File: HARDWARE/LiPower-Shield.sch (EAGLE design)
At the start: 52 parts, among them U1 MAX17043G+U, U2 TPS61200, U3 MCP73831, U4 ARDUINO_R3_SHIELD, X1 USBSMD

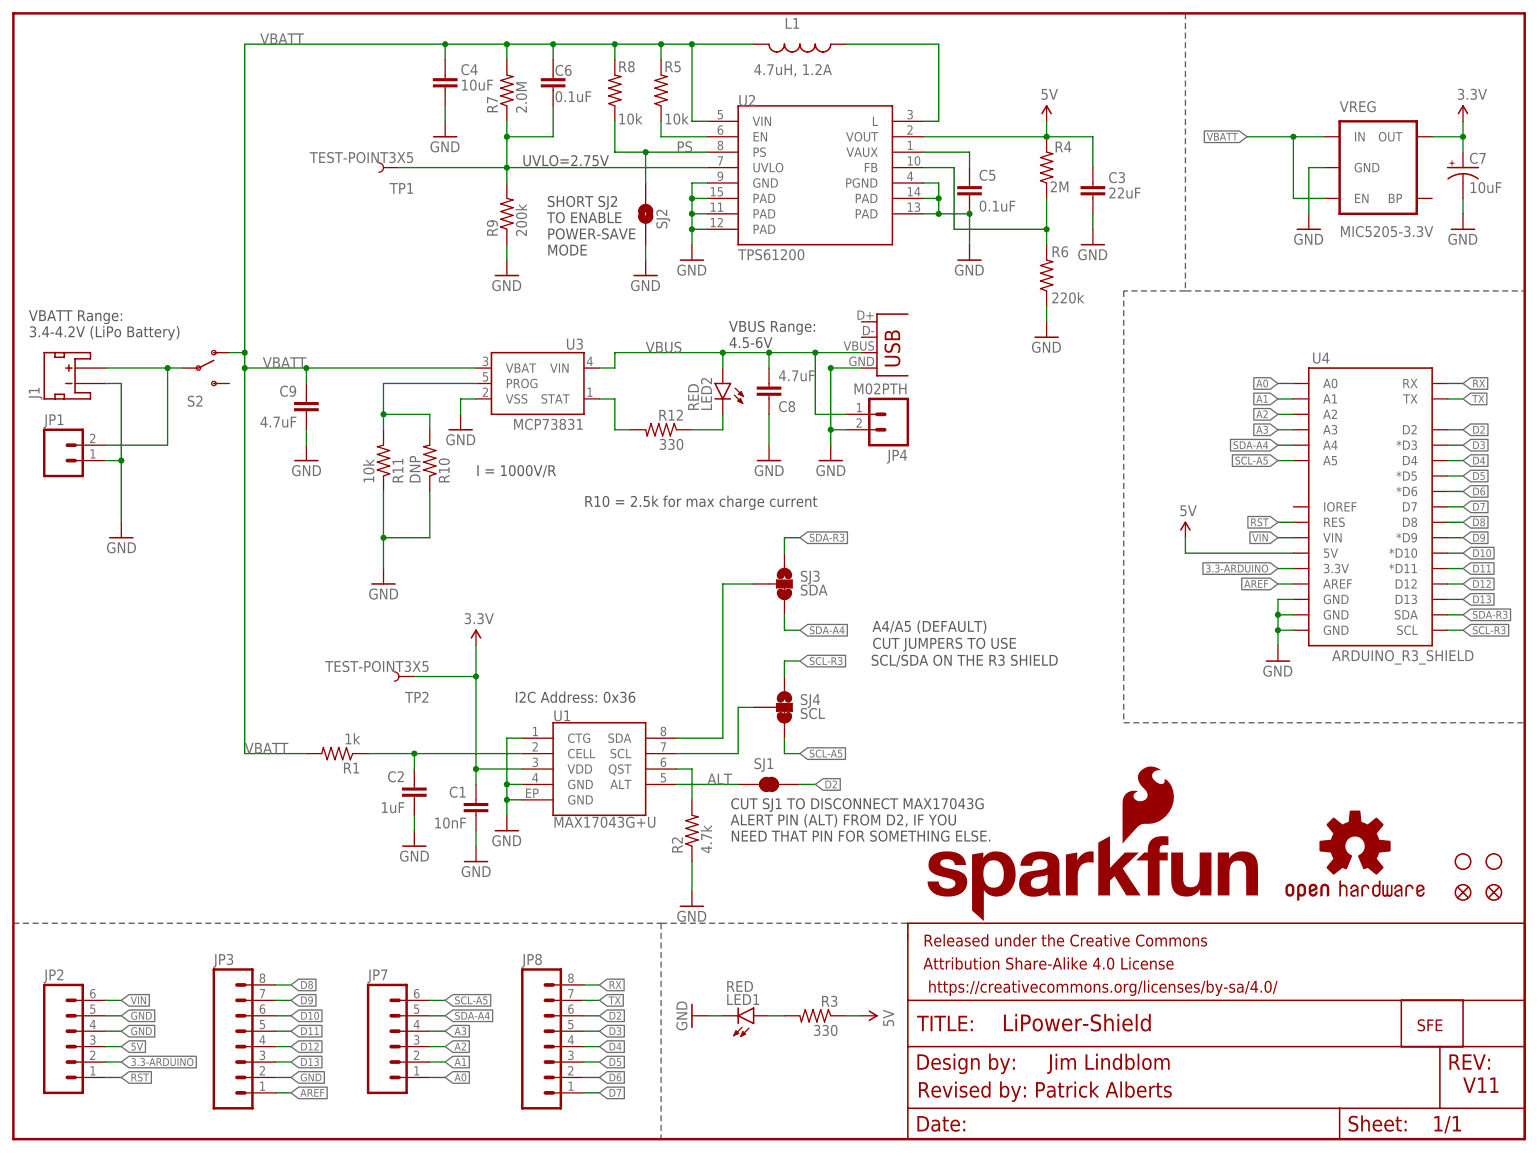
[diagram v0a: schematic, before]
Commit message: Schematic Cleanup
fixed all of these...

1) GND and 5V symbols need to be rotated "up" and "down".

2) all LEDs prefixes should be "D#"

3) R4 needs to be shifted down one grid space. The resulting 4 way
junction will need to be fixed then too.

4) J1 should have a prefix of JP#

5) USB connector is currently "X1" should be a JP prefix.

6) small flame symbol needs to be updated.
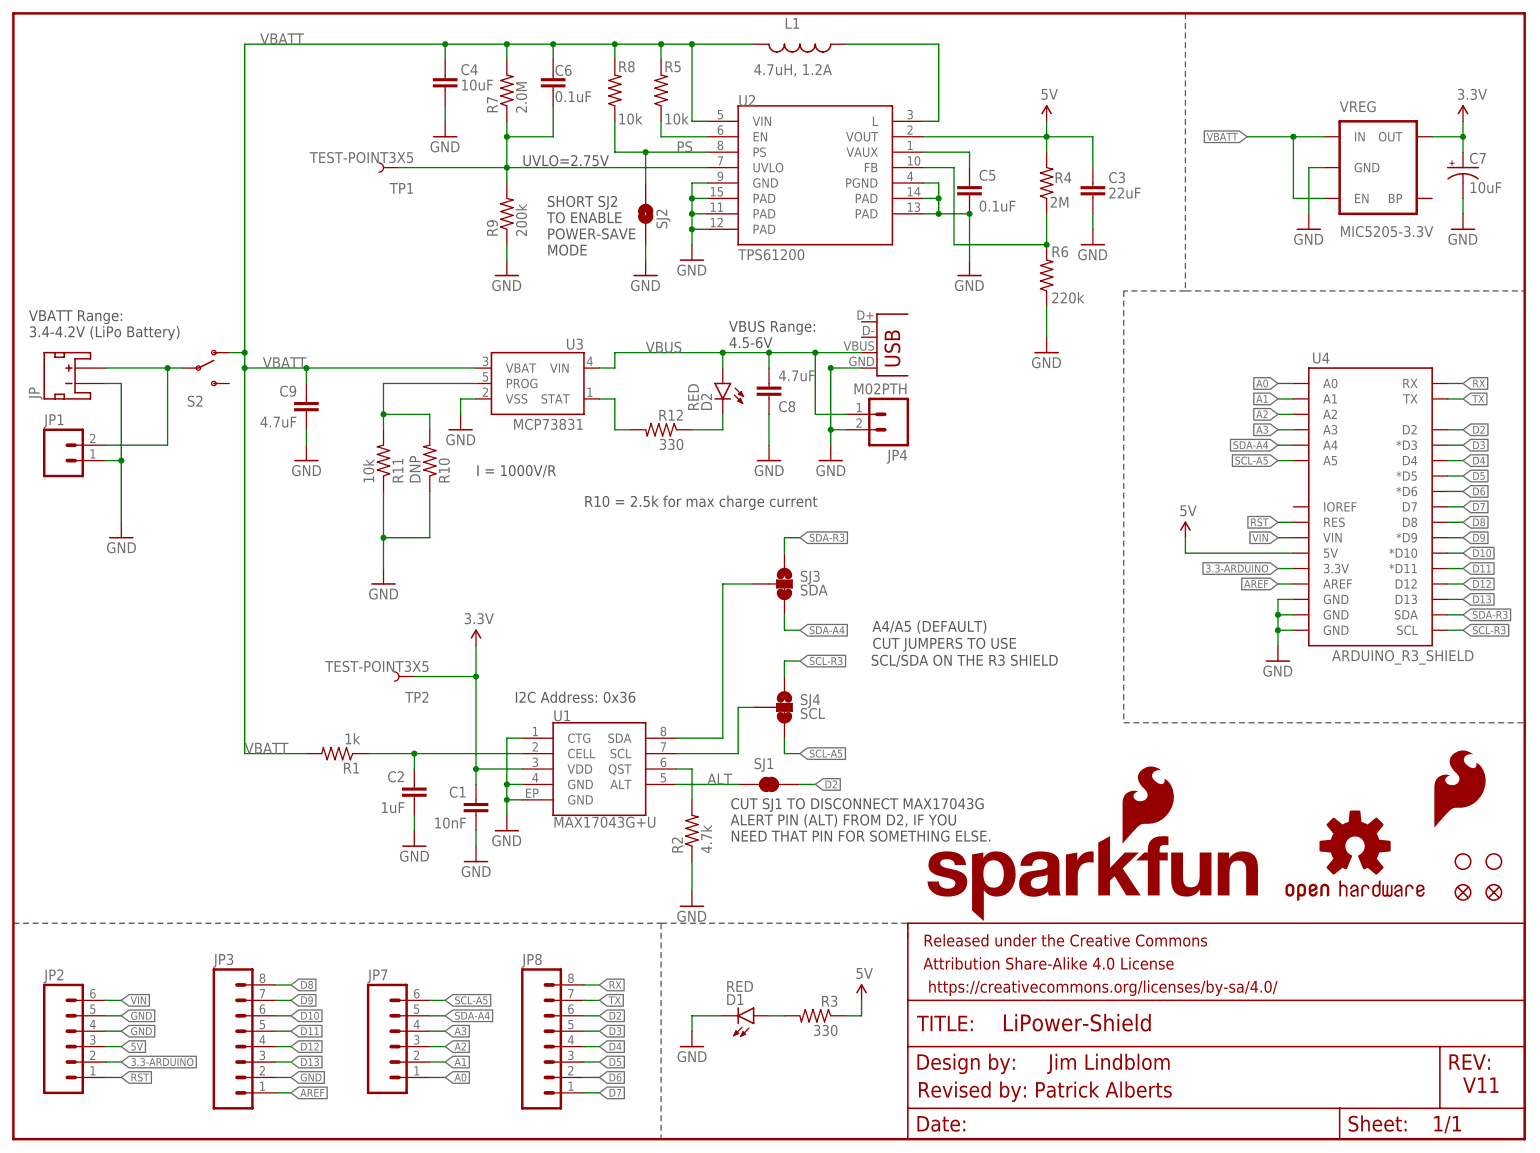
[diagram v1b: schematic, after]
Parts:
- removed JP100: LOGO-SFESK, SparkFun:LOGO-SFESK
- added LOGO3: SFE_LOGO_FLAME.1_INCH, SparkFun-Aesthetics:SFE_LOGO_FLAME.1_INCH
- renumbered J1 to JP, LED1 to D1, LED2 to D2, X1 to JP11
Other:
- moved on the sheet: R4

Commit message: changed fids to regular from micro
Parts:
- removed JP5, JP6: FIDUCIAL1X2.5, abes:FIDUCIAL1X2.5
- added FID1, FID2: FIDUCIAL1X2, SparkFun-Aesthetics:FIDUCIAL1X2
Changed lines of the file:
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@@
 <?xml version="1.0" encoding="utf-8"?>
 <!DOCTYPE eagle SYSTEM "eagle.dtd">
-<eagle version="6.4">
+<eagle version="6.6.0">
 <drawing>
 <settings>
@@
 <part name="SJ2" library="SparkFun" deviceset="SOLDERJUMPER" device="NO" value="PS"/>
 <part name="GND17" library="SparkFun" deviceset="GND" device=""/>
-<part name="JP5" library="abes" deviceset="FIDUCIAL" device="1X2.5"/>
-<part name="JP6" library="abes" deviceset="FIDUCIAL" device="1X2.5"/>
 <part name="JP" library="SparkFun-Connectors" deviceset="JST_2MM_MALE" device=""/>
 <part name="TP1" library="SparkFun-Passives" deviceset="TEST-POINT" device="3X5"/>
@@
 <part name="JP10" library="SparkFun" deviceset="STAND-OFF" device="TIGHT"/>
 <part name="LOGO3" library="SparkFun-Aesthetics" deviceset="SFE_LOGO_FLAME" device=".1_INCH"/>
+<part name="FID1" library="SparkFun-Aesthetics" deviceset="FIDUCIAL" device="1X2"/>
+<part name="FID2" library="SparkFun-Aesthetics" deviceset="FIDUCIAL" device="1X2"/>
 </parts>
 <sheets>
@@
 </instance>
 <instance part="GND17" gate="1" x="104.14" y="142.24"/>
-<instance part="JP5" gate="G$1" x="243.84" y="40.64"/>
-<instance part="JP6" gate="G$1" x="238.76" y="40.64"/>
 <instance part="JP" gate="G$1" x="10.16" y="124.46" rot="R90"/>
 <instance part="TP1" gate="G$1" x="63.5" y="160.02" rot="R180"/>
@@
 <instance part="JP10" gate="G$1" x="243.84" y="45.72"/>
 <instance part="LOGO3" gate="G$1" x="233.68" y="50.8"/>
+<instance part="FID1" gate="G$1" x="238.76" y="40.64"/>
+<instance part="FID2" gate="G$1" x="243.84" y="40.64"/>
 </instances>
 <busses>

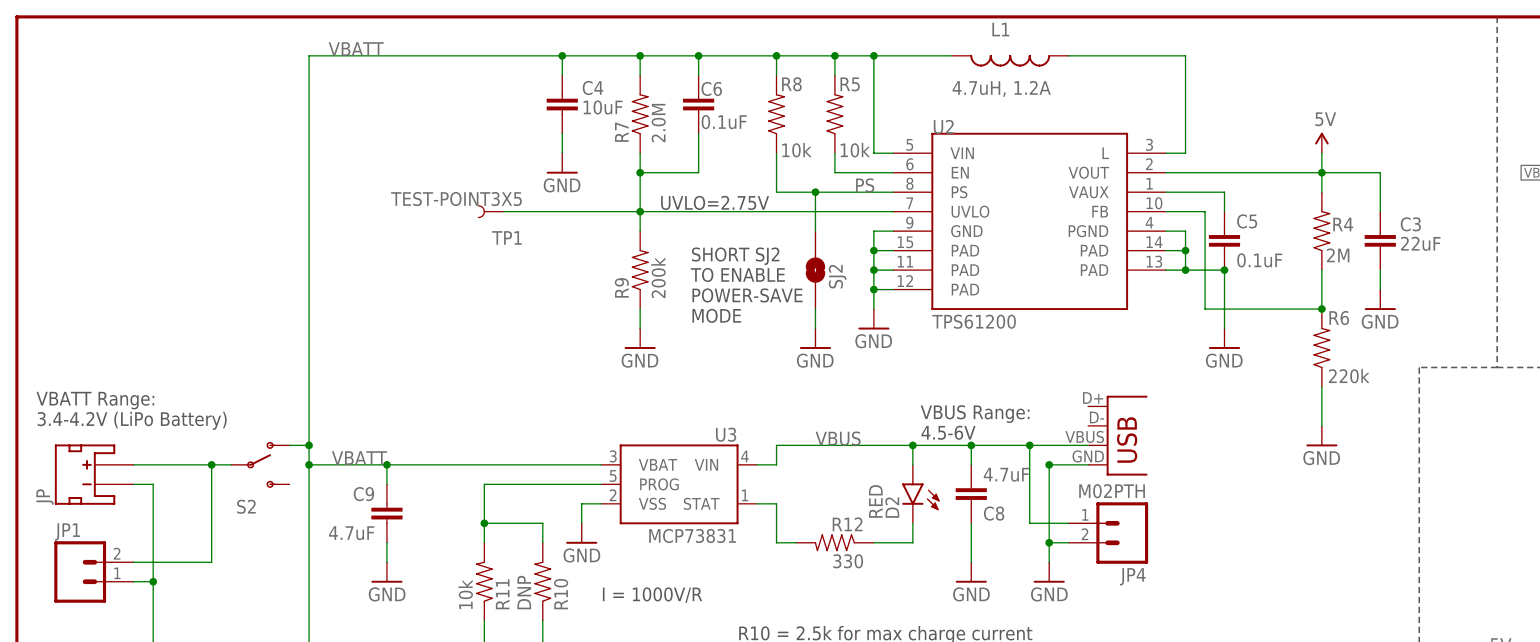
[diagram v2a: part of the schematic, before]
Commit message: Fixed current QC checklist issues.
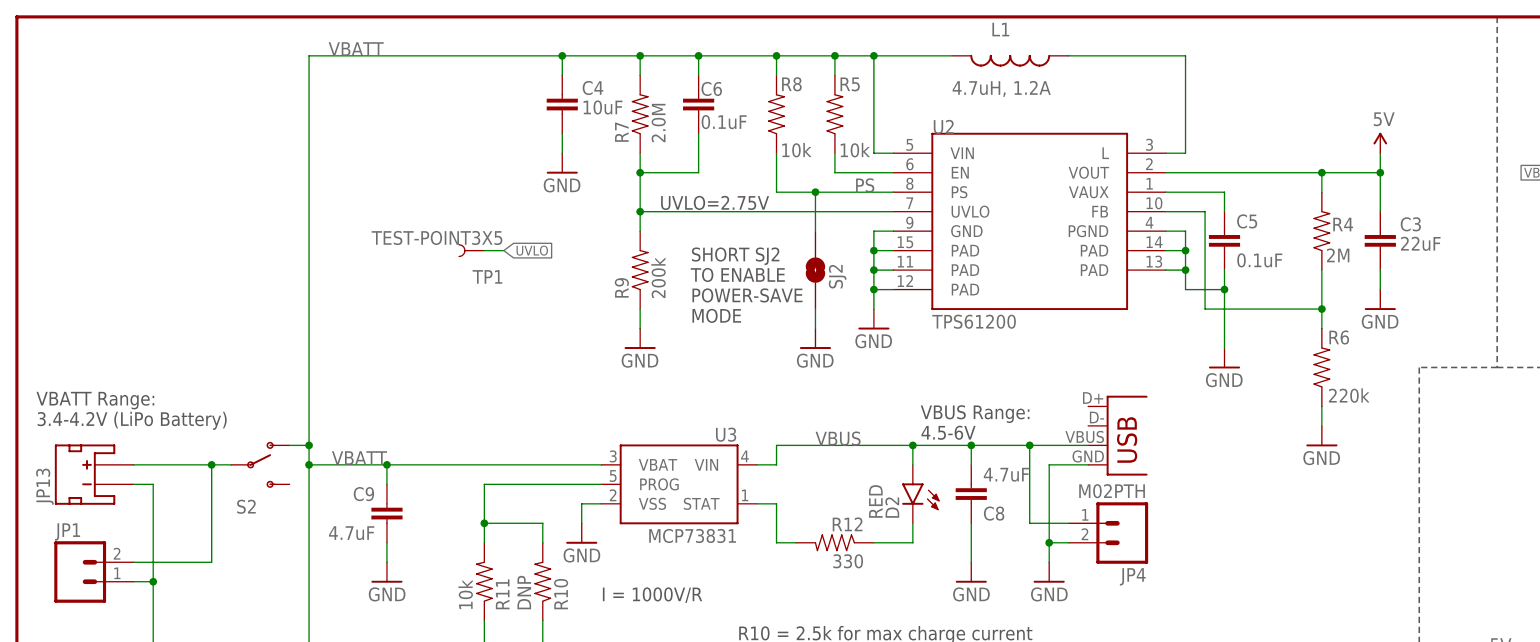
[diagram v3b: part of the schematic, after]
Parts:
- renumbered JP to JP13
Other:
- moved on the sheet: R6, TP1
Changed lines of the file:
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@@
 <?xml version="1.0" encoding="utf-8"?>
 <!DOCTYPE eagle SYSTEM "eagle.dtd">
-<eagle version="6.6.0">
+<eagle version="6.4">
 <drawing>
 <settings>
@@
 <part name="R5" library="SparkFun-Resistors" deviceset="10KOHM1/10W1%(0603)" device="0603" value="10k"/>
 <part name="R8" library="SparkFun-Resistors" deviceset="10KOHM1/10W1%(0603)" device="0603" value="10k"/>
-<part name="U$4" library="SparkFun" deviceset="5V" device=""/>
 <part name="SJ2" library="SparkFun" deviceset="SOLDERJUMPER" device="NO" value="PS"/>
 <part name="GND17" library="SparkFun" deviceset="GND" device=""/>
-<part name="JP" library="SparkFun-Connectors" deviceset="JST_2MM_MALE" device=""/>
+<part name="JP13" library="SparkFun-Connectors" deviceset="JST_2MM_MALE" device=""/>
 <part name="TP1" library="SparkFun-Passives" deviceset="TEST-POINT" device="3X5"/>
 <part name="LOGO1" library="SparkFun-Aesthetics" deviceset="OSHW-LOGO" device="S"/>
@@
 <part name="FID1" library="SparkFun-Aesthetics" deviceset="FIDUCIAL" device="1X2"/>
 <part name="FID2" library="SparkFun-Aesthetics" deviceset="FIDUCIAL" device="1X2"/>
+<part name="U$2" library="SparkFun" deviceset="5V" device=""/>
 </parts>
 <sheets>
@@
 </instance>
 <instance part="C5" gate="G$1" x="157.48" y="154.94"/>
-<instance part="R6" gate="G$1" x="170.18" y="142.24" smashed="yes" rot="R90">
-<attribute name="NAME" x="170.942" y="145.2626" size="1.778" layer="95"/>
-<attribute name="VALUE" x="170.942" y="137.668" size="1.778" layer="96"/>
+<instance part="R6" gate="G$1" x="170.18" y="139.7" smashed="yes" rot="R90">
+<attribute name="NAME" x="170.942" y="142.7226" size="1.778" layer="95"/>
+<attribute name="VALUE" x="170.942" y="135.128" size="1.778" layer="96"/>
 </instance>
 <instance part="GND4" gate="1" x="177.8" y="147.32"/>
@@
 <attribute name="VALUE" x="73.66" y="172.72" size="1.778" layer="96"/>
 </instance>
-<instance part="GND5" gate="1" x="157.48" y="142.24"/>
+<instance part="GND5" gate="1" x="157.48" y="139.7"/>
 <instance part="GND6" gate="1" x="111.76" y="144.78"/>
 <instance part="GND16" gate="1" x="71.12" y="165.1"/>
@@
 <attribute name="VALUE" x="99.568" y="167.132" size="1.778" layer="96"/>
 </instance>
-<instance part="U$4" gate="G$1" x="170.18" y="167.64"/>
 <instance part="SJ2" gate="1" x="104.14" y="152.4" smashed="yes" rot="R90">
 <attribute name="NAME" x="107.696" y="149.86" size="1.778" layer="95" rot="R90"/>
 </instance>
 <instance part="GND17" gate="1" x="104.14" y="142.24"/>
-<instance part="JP" gate="G$1" x="10.16" y="124.46" rot="R90"/>
-<instance part="TP1" gate="G$1" x="63.5" y="160.02" rot="R180"/>
+<instance part="JP13" gate="G$1" x="10.16" y="124.46" rot="R90"/>
+<instance part="TP1" gate="G$1" x="60.96" y="154.94" rot="R180"/>
 <instance part="LOGO1" gate="G$1" x="220.98" y="48.26"/>
 <instance part="LOGO2" gate="G$1" x="149.86" y="35.56"/>
@@
 <instance part="FID1" gate="G$1" x="238.76" y="40.64"/>
 <instance part="FID2" gate="G$1" x="243.84" y="40.64"/>
+<instance part="U$2" gate="G$1" x="177.8" y="167.64"/>
 </instances>
 <busses>
@@
 <wire x1="134.62" y1="116.84" x2="134.62" y2="127" width="0.1524" layer="91"/>
 <wire x1="137.16" y1="116.84" x2="134.62" y2="116.84" width="0.1524" layer="91"/>
-<junction x="134.62" y="127"/>
 <junction x="134.62" y="116.84"/>
 <pinref part="JP11" gate="G$1" pin="GND"/>
@@
 <pinref part="GND13" gate="1" pin="GND"/>
 <pinref part="JP1" gate="G$1" pin="1"/>
-<pinref part="JP" gate="G$1" pin="-"/>
+<pinref part="JP13" gate="G$1" pin="-"/>
 </segment>
 <segment>
@@
 <wire x1="152.4" y1="154.94" x2="152.4" y2="152.4" width="0.1524" layer="91"/>
 <wire x1="149.86" y1="152.4" x2="152.4" y2="152.4" width="0.1524" layer="91"/>
-<wire x1="157.48" y1="152.4" x2="157.48" y2="144.78" width="0.1524" layer="91"/>
-<wire x1="152.4" y1="152.4" x2="157.48" y2="152.4" width="0.1524" layer="91"/>
+<wire x1="157.48" y1="152.4" x2="157.48" y2="149.86" width="0.1524" layer="91"/>
+<wire x1="157.48" y1="149.86" x2="157.48" y2="142.24" width="0.1524" layer="91"/>
 <junction x="152.4" y="154.94"/>
 <junction x="152.4" y="152.4"/>
-<junction x="157.48" y="152.4"/>
 <pinref part="U2" gate="G$1" pin="PGND"/>
 <pinref part="U2" gate="G$1" pin="PAD@5"/>
@@
 <pinref part="C5" gate="G$1" pin="2"/>
 <pinref part="GND5" gate="1" pin="GND"/>
+<wire x1="152.4" y1="152.4" x2="152.4" y2="149.86" width="0.1524" layer="91"/>
+<wire x1="152.4" y1="149.86" x2="157.48" y2="149.86" width="0.1524" layer="91"/>
+<junction x="157.48" y="149.86"/>
 </segment>
 <segment>
@@
 </segment>
 <segment>
-<wire x1="170.18" y1="132.08" x2="170.18" y2="137.16" width="0.1524" layer="91"/>
+<wire x1="170.18" y1="132.08" x2="170.18" y2="134.62" width="0.1524" layer="91"/>
 <pinref part="R6" gate="G$1" pin="1"/>
 <pinref part="GND21" gate="1" pin="GND"/>
@@
 </segment>
 <segment>
-<pinref part="U$4" gate="G$1" pin="5V"/>
 <wire x1="170.18" y1="162.56" x2="170.18" y2="165.1" width="0.1524" layer="91"/>
 <pinref part="R4" gate="G$1" pin="2"/>
 <pinref part="U2" gate="G$1" pin="VOUT"/>
-<wire x1="170.18" y1="165.1" x2="170.18" y2="167.64" width="0.1524" layer="91"/>
 <wire x1="149.86" y1="165.1" x2="170.18" y2="165.1" width="0.1524" layer="91"/>
 <junction x="170.18" y="165.1"/>
@@
 <pinref part="C3" gate="G$1" pin="1"/>
 <wire x1="177.8" y1="165.1" x2="170.18" y2="165.1" width="0.1524" layer="91"/>
+<pinref part="U$2" gate="G$1" pin="5V"/>
+<wire x1="177.8" y1="165.1" x2="177.8" y2="167.64" width="0.1524" layer="91"/>
+<junction x="177.8" y="165.1"/>
 </segment>
 <segment>
@@
 <pinref part="U2" gate="G$1" pin="UVLO"/>
 <pinref part="C6" gate="G$1" pin="2"/>
-<pinref part="TP1" gate="G$1" pin="1"/>
-<wire x1="63.5" y1="160.02" x2="81.28" y2="160.02" width="0.1524" layer="91"/>
 <pinref part="R9" gate="G$1" pin="2"/>
 <pinref part="R7" gate="G$1" pin="1"/>
 </segment>
+<segment>
+<pinref part="TP1" gate="G$1" pin="1"/>
+<wire x1="60.96" y1="154.94" x2="63.5" y2="154.94" width="0.1524" layer="91"/>
+<label x="63.5" y="154.94" size="1.27" layer="95" xref="yes"/>
+</segment>
 </net>
 <net name="FB" class="0">
@@
 <wire x1="154.94" y1="160.02" x2="149.86" y2="160.02" width="0.1524" layer="91"/>
 <wire x1="154.94" y1="147.32" x2="154.94" y2="160.02" width="0.1524" layer="91"/>
+<wire x1="170.18" y1="144.78" x2="170.18" y2="147.32" width="0.1524" layer="91"/>
 <wire x1="170.18" y1="147.32" x2="170.18" y2="152.4" width="0.1524" layer="91"/>
-<wire x1="154.94" y1="147.32" x2="170.18" y2="147.32" width="0.1524" layer="91"/>
-<junction x="170.18" y="147.32"/>
 <pinref part="U2" gate="G$1" pin="FB"/>
 <pinref part="R6" gate="G$1" pin="2"/>
 <pinref part="R4" gate="G$1" pin="1"/>
+<wire x1="154.94" y1="147.32" x2="170.18" y2="147.32" width="0.1524" layer="91"/>
+<junction x="170.18" y="147.32"/>
 </segment>
 </net>
@@
 <net name="N$7" class="0">
 <segment>
-<pinref part="JP" gate="G$1" pin="+"/>
+<pinref part="JP13" gate="G$1" pin="+"/>
 <wire x1="15.24" y1="127" x2="25.4" y2="127" width="0.1524" layer="91"/>
 <wire x1="25.4" y1="127" x2="25.4" y2="114.3" width="0.1524" layer="91"/>
